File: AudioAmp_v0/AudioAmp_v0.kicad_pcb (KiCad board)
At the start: 2 copper layers, 95 x 72 mm, 4 parts

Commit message: 最低限完成
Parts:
- added C1: 100u, Capacitor_SMD:CP_Elec_6.3x5.7, F.Cu at (15.2, 15.9)
- added C10: 0.1u, Capacitor_THT:C_Rect_L13.0mm_W6.0mm_P10.00mm_FKS3_FKP3_MKS4, F.Cu at (170.3, 19.5)
- added C11: 0.1u, Capacitor_THT:C_Rect_L13.0mm_W6.0mm_P10.00mm_FKS3_FKP3_MKS4, F.Cu at (170.3, 27.0)
- added C12: 0.1u, Capacitor_SMD:C_0603_1608Metric, F.Cu at (63.5, 14.0)
- added C13: 0.1u, Capacitor_SMD:C_0603_1608Metric, F.Cu at (137.2, 86.3)
- added C14: ~, Capacitor_SMD:C_0805_2012Metric, F.Cu at (10.8, 27.9)
- added C15: ~, Capacitor_SMD:C_0805_2012Metric, F.Cu at (31.1, 30.5)
- added C16: ~, Capacitor_SMD:C_0805_2012Metric, F.Cu at (39.4, 38.7)
- added C17: ~, Capacitor_SMD:C_0805_2012Metric, F.Cu at (25.4, 51.8)
- added C18: 100u, Capacitor_SMD:CP_Elec_6.3x5.7, F.Cu at (16.5, 38.1)
- added C19: 100u, Capacitor_SMD:CP_Elec_6.3x5.7, F.Cu at (16.5, 47.6)
- added C2: 10u, Capacitor_SMD:C_0805_2012Metric, F.Cu at (22.2, 13.8)
- added C3: 0.1u, Capacitor_SMD:C_0603_1608Metric, F.Cu at (22.2, 11.9)
- added C4: 2.2u, Capacitor_THT:C_Axial_L17.0mm_D7.0mm_P20.00mm_Horizontal, F.Cu at (45.7, 51.9)
- added C5: 2.2u, Capacitor_THT:C_Axial_L17.0mm_D7.0mm_P20.00mm_Horizontal, F.Cu at (53.3, 54.5)
- added C6: 0.1u, Capacitor_SMD:C_0603_1608Metric, F.Cu at (28.4, 12.1)
- added C7: 0.1u, Capacitor_SMD:C_0603_1608Metric, F.Cu at (33.6, 12.0)
- added C8: 10u, Capacitor_SMD:C_0805_2012Metric, F.Cu at (28.4, 13.9)
- added C9: 10u, Capacitor_SMD:C_0805_2012Metric, F.Cu at (33.6, 13.8)
- added J1: AudioJack3, Connector_Audio:Jack_3.5mm_Switronic_ST-005-G_horizontal, F.Cu at (15.2, 63.5)
- added J2: Conn_01x02_Pin, Connector_Molex:Molex_SPOX_5268-02A_1x02_P2.50mm_Horizontal, F.Cu at (7.62, 12.7)
- added J3: Connector_RCJ-042, TomoshibiLibrary:Connector_RCJ-042CUD, F.Cu at (25.4, 62.3)
- added J4: Connector_RCJ-042, TomoshibiLibrary:Connector_RCJ-042CUD, F.Cu at (38.1, 62.3)
- added J5: AudioJack3, Connector_Audio:Jack_3.5mm_Switronic_ST-005-G_horizontal, F.Cu at (78.7, 63.5)
- added J6: Conn_01x02_Pin, Connector_JST:JST_XH_S2B-XH-A_1x02_P2.50mm_Horizontal, F.Cu at (9.80, 36.9)
- added J7: Conn_01x02_Pin, Connector_JST:JST_XH_S2B-XH-A_1x02_P2.50mm_Horizontal, F.Cu at (9.80, 45.7)
- added Q1: NMOS_ MTB7D0N6RJ3, Package_TO_SOT_SMD:TO-252-2, F.Cu at (26.7, 38.4)
- added Q2: PMOS_MTP4835I3, Package_TO_SOT_SMD:TO-252-2, F.Cu at (24.1, 30.7)
- added Q3: NMOS_BSS138, Package_TO_SOT_SMD:SOT-23, F.Cu at (34.9, 39.4)
- added Q4: PMOS_BSS84, Package_TO_SOT_SMD:TSOT-23, F.Cu at (15.7, 28.8)
- added Q5: PMOS_BSS84, Package_TO_SOT_SMD:TSOT-23, F.Cu at (31.1, 23.5)
- added Q6: PMOS_MTP4835I3, Package_TO_SOT_SMD:TO-252-2, F.Cu at (22.3, 23.2)
- added Q7: NMOS_BSS138, Package_TO_SOT_SMD:SOT-23, F.Cu at (21.9, 44.5)
- added Q8: NMOS_ MTB7D0N6RJ3, Package_TO_SOT_SMD:TO-252-2, F.Cu at (30.3, 45.5)
- added R1: 1K, Resistor_THT:R_Axial_DIN0207_L6.3mm_D2.5mm_P10.16mm_Horizontal, F.Cu at (45.7, 27.9)
- added R10: 27K, Resistor_THT:R_Axial_DIN0207_L6.3mm_D2.5mm_P10.16mm_Horizontal, F.Cu at (114.1, 54.2)
- added R11: 47, Resistor_THT:R_Axial_DIN0207_L6.3mm_D2.5mm_P10.16mm_Horizontal, F.Cu at (63.5, 38.1)
- added R12: 47, Resistor_THT:R_Axial_DIN0207_L6.3mm_D2.5mm_P10.16mm_Horizontal, F.Cu at (114.1, 62.3)
- added R13: 47, Resistor_THT:R_Axial_DIN0207_L6.3mm_D2.5mm_P10.16mm_Horizontal, F.Cu at (68.6, 30.5)
- added R14: 47, Resistor_THT:R_Axial_DIN0207_L6.3mm_D2.5mm_P10.16mm_Horizontal, F.Cu at (114.1, 70.4)
- added R15: 22, Resistor_THT:R_Axial_DIN0207_L6.3mm_D2.5mm_P10.16mm_Horizontal, F.Cu at (85.1, 63.5)
- added R16: 22, Resistor_THT:R_Axial_DIN0207_L6.3mm_D2.5mm_P10.16mm_Horizontal, F.Cu at (72.4, 59.7)
- added R17: 10K, Resistor_SMD:R_0603_1608Metric, F.Cu at (28.4, 15.9)
- added R18: 10K, Resistor_SMD:R_0603_1608Metric, F.Cu at (33.6, 15.8)
- added R19: 100K, Resistor_SMD:R_0603_1608Metric, F.Cu at (12.9, 27.8)
- added R2: 1K, Resistor_THT:R_Axial_DIN0207_L6.3mm_D2.5mm_P10.16mm_Horizontal, F.Cu at (114.1, 21.8)
- added R20: 10k, Resistor_SMD:R_0603_1608Metric, F.Cu at (16.5, 24.8)
- added R21: 10K, Resistor_SMD:R_0603_1608Metric, F.Cu at (15.7, 31.9)
- added R22: 10K, Resistor_SMD:R_0603_1608Metric, F.Cu at (31.1, 20.3)
- added R23: 100K, Resistor_SMD:R_0603_1608Metric, F.Cu at (31.1, 26.7)
- added R24: 10k, Resistor_SMD:R_0603_1608Metric, F.Cu at (31.1, 28.6)
- added R25: 10K, Resistor_SMD:R_0603_1608Metric, F.Cu at (34.9, 36.2)
- added R26: 100K, Resistor_SMD:R_0603_1608Metric, F.Cu at (37.5, 38.7)
- added R27: 10k, Resistor_SMD:R_0603_1608Metric, F.Cu at (36.7, 42.2)
- added R28: 10K, Resistor_SMD:R_0603_1608Metric, F.Cu at (21.9, 47.6)
- added R29: 100K, Resistor_SMD:R_0603_1608Metric, F.Cu at (25.4, 50.0)
- added R3: 22K, Resistor_THT:R_Axial_DIN0207_L6.3mm_D2.5mm_P10.16mm_Horizontal, F.Cu at (49.5, 27.9)
- added R30: 10k, Resistor_SMD:R_0603_1608Metric, F.Cu at (21.0, 40.0)
- added R4: 22K, Resistor_THT:R_Axial_DIN0207_L6.3mm_D2.5mm_P10.16mm_Horizontal, F.Cu at (114.1, 29.9)
- added R5: 2.2K, Resistor_THT:R_Axial_DIN0207_L6.3mm_D2.5mm_P10.16mm_Horizontal, F.Cu at (53.3, 27.9)
- added R6: 2.2K, Resistor_THT:R_Axial_DIN0207_L6.3mm_D2.5mm_P10.16mm_Horizontal, F.Cu at (114.1, 38.0)
- added R7: 10K, Resistor_THT:R_Axial_DIN0207_L6.3mm_D2.5mm_P10.16mm_Horizontal, F.Cu at (87.6, 33.0)
- added R8: 10K, Resistor_THT:R_Axial_DIN0207_L6.3mm_D2.5mm_P10.16mm_Horizontal, F.Cu at (114.1, 46.1)
- added R9: 27K, Resistor_THT:R_Axial_DIN0207_L6.3mm_D2.5mm_P10.16mm_Horizontal, F.Cu at (73.7, 21.6)
- added RV1: R_Potentiometer_Dual, TomoshibiLibrary:VR_ALPS9-dual, F.Cu at (55.5, 65.9)
- added SW1: SW_DPDT_x2, Button_Switch_THT:SW_CK_JS202011CQN_DPDT_Straight, F.Cu at (5.84, 22.9)
- added SW2: SW_DPDT_x2, Button_Switch_THT:SW_E-Switch_EG2219_DPDT_Angled, F.Cu at (60.8, 64.8)
- added U1: MAU108, TomoshibiLibrary:DCDC_MAUseries, F.Cu at (18.8, 4.63)
- added U2: NJM5532, Package_DIP:DIP-8_W7.62mm, F.Cu at (58.4, 19.1)
- added U3: NJM5532, Package_DIP:DIP-8_W7.62mm, F.Cu at (177.4, 73.9)
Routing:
- net Net-(J1-PadT): track 0.00 -> 40.3 mm
- net -12V: track 0.00 -> 40.3 mm
- net Net-(Q3-G): track 0.00 -> 40.2 mm, vias 0 -> 1
- net Net-(J1-PadR): track 0.00 -> 38.0 mm
- net Net-(Q7-G): track 0.00 -> 37.9 mm, vias 0 -> 1
- net Net-(Q5-G): track 0.00 -> 28.8 mm, vias 0 -> 1
- net +12V: track 0.00 -> 28.5 mm
- net +9V: track 0.00 -> 27.6 mm
- net -9V: track 0.00 -> 24.8 mm
- net Net-(Q7-D): track 0.00 -> 16.3 mm
- net GND: track 0.00 -> 15.0 mm
- net Net-(Q4-G): track 0.00 -> 11.7 mm
- net Net-(Q5-D): track 0.00 -> 10.9 mm
- net Net-(Q2-G): track 0.00 -> 10.8 mm
- net Net-(Q1-G): track 0.00 -> 10.4 mm
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- added copper zone on F.Cu, net +5V

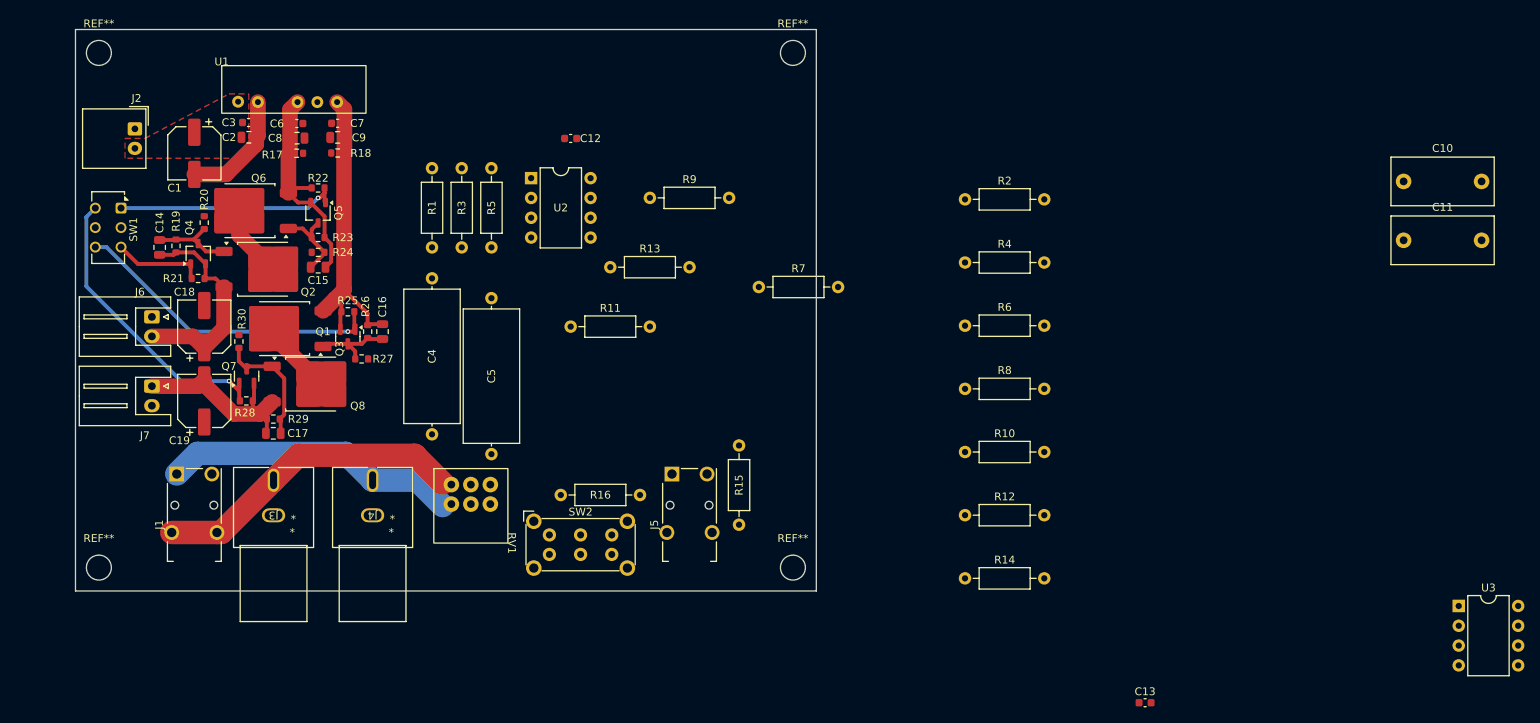
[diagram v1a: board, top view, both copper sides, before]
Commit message: LED追加
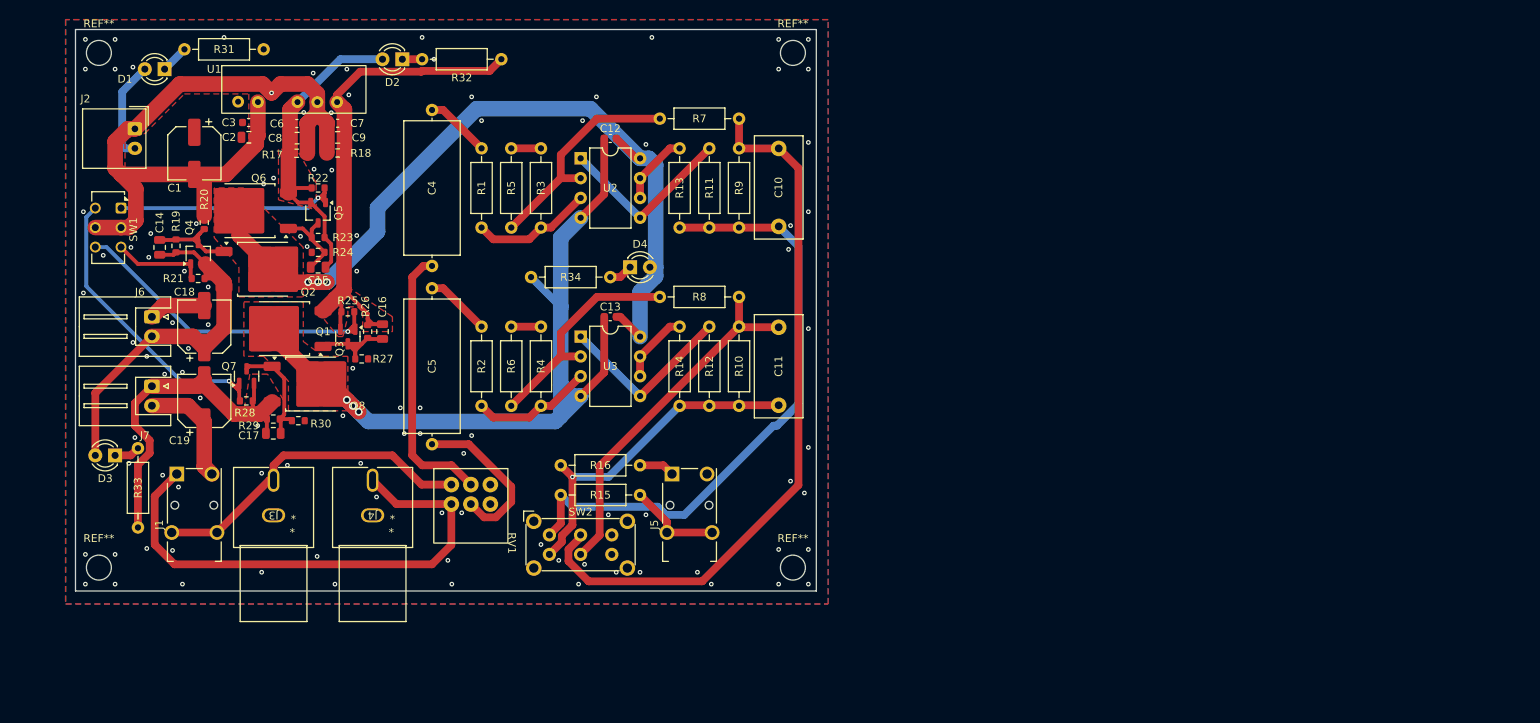
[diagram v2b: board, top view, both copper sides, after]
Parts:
- added D1: LED, LED_THT:LED_D3.0mm, F.Cu at (11.4, 5.08)
- added D2: LED, LED_THT:LED_D3.0mm, F.Cu at (41.9, 3.81)
- added D3: LED, LED_THT:LED_D3.0mm, F.Cu at (5.08, 54.6)
- added D4: LED, LED_THT:LED_D3.0mm, F.Cu at (71.1, 30.5)
- added R31: 10K, Resistor_THT:R_Axial_DIN0207_L6.3mm_D2.5mm_P10.16mm_Horizontal, F.Cu at (24.1, 2.54)
- added R32: 10K, Resistor_THT:R_Axial_DIN0207_L6.3mm_D2.5mm_P10.16mm_Horizontal, F.Cu at (54.6, 3.81)
- added R33: 10K, Resistor_THT:R_Axial_DIN0207_L6.3mm_D2.5mm_P10.16mm_Horizontal, F.Cu at (8.01, 63.9)
- added R34: 10K, Resistor_THT:R_Axial_DIN0207_L6.3mm_D2.5mm_P10.16mm_Horizontal, F.Cu at (58.4, 31.8)
- moved U3 117.8 mm to (64.8, 39.4)
- moved C13 84.6 mm to (68.6, 36.8), turned to 180 degrees
- moved C11 80.9 mm to (90.2, 38.2), turned to -90 degrees
- moved C10 80.2 mm to (90.2, 15.2), turned to -90 degrees
- moved R2 64.1 mm to (52.1, 38.1), turned to -90 degrees
- moved R6 58.2 mm to (55.9, 38.1), turned to -90 degrees
- moved R4 55.0 mm to (59.7, 38.1), turned to -90 degrees
- moved R14 42.8 mm to (77.5, 48.3), turned to 90 degrees
- moved R12 35.7 mm to (81.3, 48.3), turned to 90 degrees
- moved R8 31.3 mm to (85.1, 34.3), turned to 180 degrees
- moved R10 29.6 mm to (85.1, 48.3), turned to 90 degrees
- moved R11 21.8 mm to (81.3, 25.4), turned to 90 degrees
- moved R7 21.7 mm to (85.1, 11.4), turned to 180 degrees
- moved C4 21.6 mm to (45.7, 30.3)
- moved R3 16.3 mm to (59.7, 15.2), turned to -90 degrees
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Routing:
- net GND: track 15.0 -> 120.9 mm, vias 0 -> 102
- net VCC: track 9.30 -> 107.2 mm, vias 0 -> 3
- net VEE: track 9.62 -> 107.2 mm, vias 0 -> 3
- net Net-(SW2A-B): track 0.00 -> 92.8 mm
- net Net-(SW2A-A): track 0.00 -> 79.8 mm
- net Net-(SW2B-B): track 0.00 -> 46.5 mm
- net Net-(SW2B-A): track 0.00 -> 43.5 mm, vias 0 -> 1
- net Net-(C4-Pad1): track 0.00 -> 35.1 mm
- net Net-(U3A--): track 0.00 -> 30.9 mm
- net Net-(U2A--): track 0.00 -> 29.1 mm
- net Net-(J1-PadR): track 38.0 -> 66.9 mm
- net -12V: track 40.3 -> 65.1 mm
- net Net-(U3B-+): track 0.00 -> 23.4 mm
- net Net-(U2B-+): track 0.00 -> 23.4 mm
- net +9V: track 27.6 -> 49.8 mm
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- added copper zone on F.Cu, net +12V
- added copper zone on F.Cu, net -12V
- added copper zone on F.Cu, net -9V
- added copper zone on B.Cu, net GND
- added copper zone on F.Cu, net GND
- added copper zone on F.Cu, net VCC
- added copper zone on F.Cu, net VEE

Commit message: シルク追加
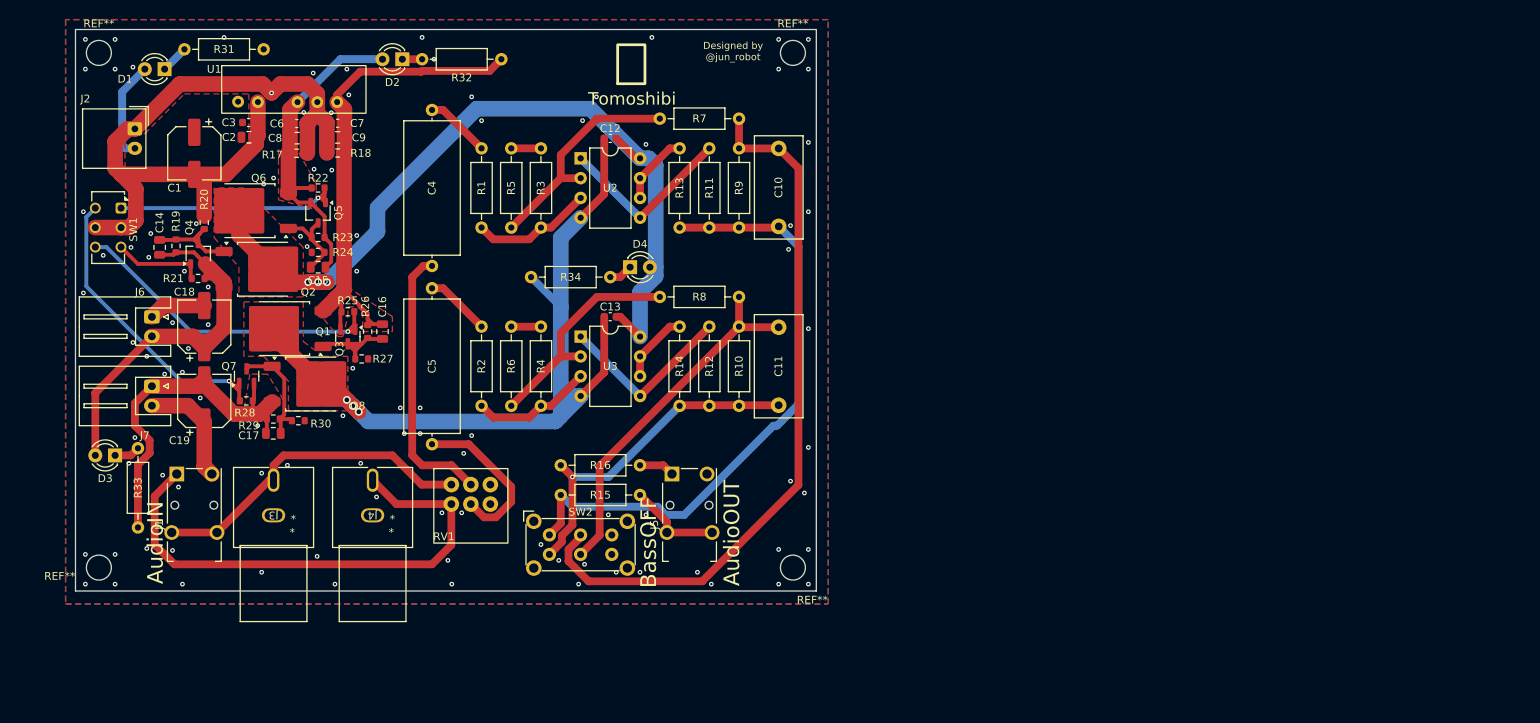
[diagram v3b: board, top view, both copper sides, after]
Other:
- board text added: "AudioIN"
- board text added: "AudioOUT"
- board text added: "BassOFF"
- board text added: "Designed by @jun_robot"
- board text added: "Tomoshibi"
- board text added: "燈"
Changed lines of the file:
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@@
     (tags "mounting hole 3.2mm no annular m3 iso14580")
     (attr exclude_from_pos_files exclude_from_bom)
-    (fp_text reference "REF**" (at 0 -3.75) (layer "F.SilkS")
+    (fp_text reference "REF**" (at -5.032 1.104) (layer "F.SilkS")
         (effects (font (size 1 1) (thickness 0.15)))
     )
@@
     (property "ki_keywords" "resistor variable")
     (attr through_hole)
-    (fp_text reference "RV1" (at 0 -0.5 -90 unlocked) (layer "F.SilkS")
+    (fp_text reference "RV1" (at -0.831 8.206 unlocked) (layer "F.SilkS")
         (effects (font (size 1 1) (thickness 0.1)))
     )
@@
     (tags "mounting hole 3.2mm no annular m3 iso14580")
     (attr exclude_from_pos_files exclude_from_bom)
-    (fp_text reference "REF**" (at 0 -3.75) (layer "F.SilkS")
+    (fp_text reference "REF**" (at 2.488 4.152) (layer "F.SilkS")
         (effects (font (size 1 1) (thickness 0.15)))
     )
@@
   (gr_rect (start 0 0) (end 95 72)
     (stroke (width 0.05) (type default)) (fill none) (layer "Edge.Cuts"))
+  (gr_text "AudioIN" (at 11.43 71.12 90) (layer "F.SilkS" knockout)
+    (effects (font (size 2 2) (thickness 0.3)) (justify left bottom))
+  )
+  (gr_text "Designed by\n@jun_robot" (at 84.328 2.794) (layer "F.SilkS")
+    (effects (font (size 0.9 0.9) (thickness 0.11)))
+  )
+  (gr_text "BassOFF\n" (at 74.676 71.628 90) (layer "F.SilkS" knockout)
+    (effects (font (size 2 2) (thickness 0.3)) (justify left bottom))
+  )
+  (gr_text "燈" (at 71.274 4.64) (layer "F.SilkS")
+    (effects (font (size 5 5) (thickness 0.35)))
+  )
+  (gr_text "AudioOUT" (at 85.344 71.374 90) (layer "F.SilkS" knockout)
+    (effects (font (size 2 2) (thickness 0.3)) (justify left bottom))
+  )
+  (gr_text "Tomoshibi" (at 71.374 8.89) (layer "F.SilkS")
+    (effects (font (size 1.6 1.6) (thickness 0.21)))
+  )
   (segment (start 8.89 5.08) (end 5.995 7.975) (width 1) (layer "B.Cu") (net 1))
   (segment (start 5.995 14.885) (end 6.35 15.24) (width 1) (layer "B.Cu") (net 1))

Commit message: 電源切り替えスイッチ修正
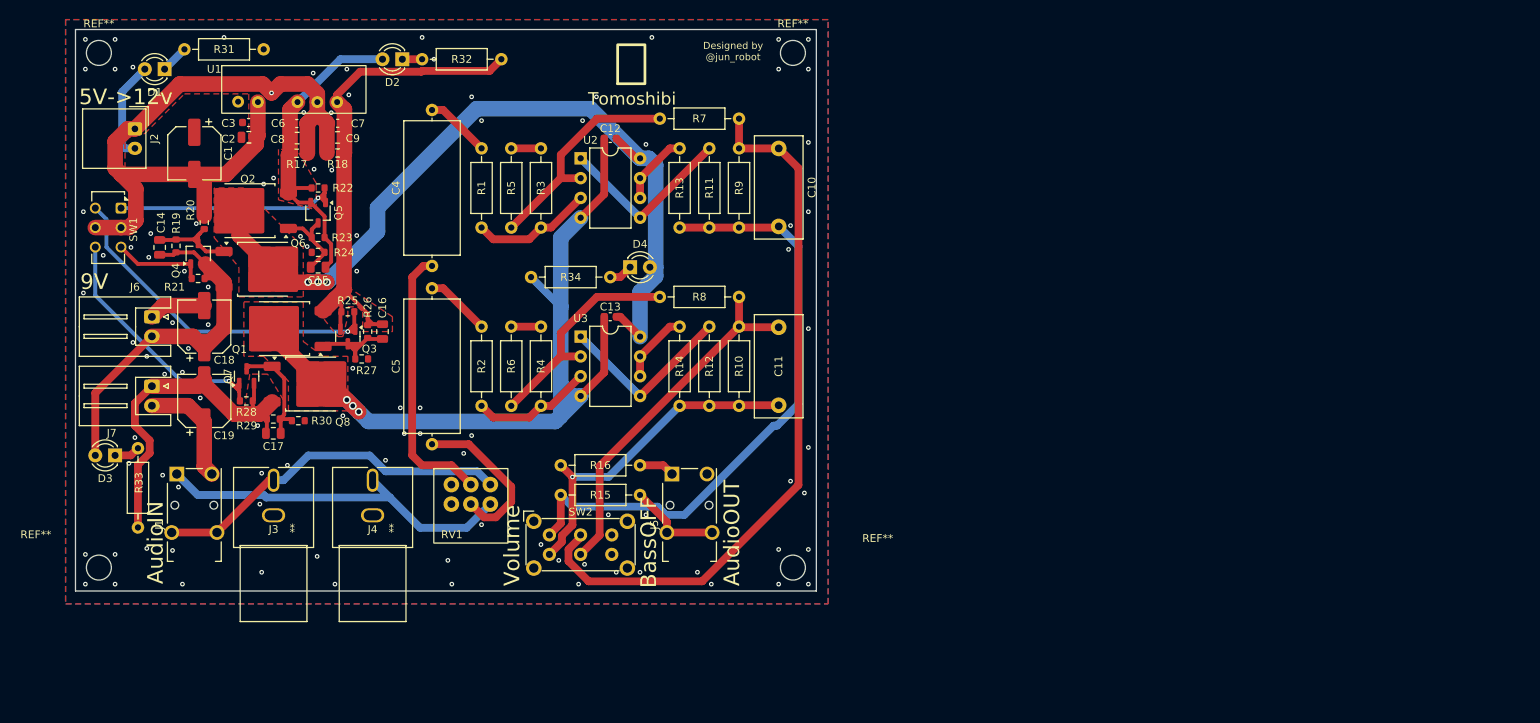
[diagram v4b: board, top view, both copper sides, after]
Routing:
- net Net-(J1-PadR): track 66.9 -> 47.5 mm
- net Net-(Q7-G): track 38.7 -> 32.8 mm
- net Net-(Q3-G): track 41.3 -> 45.5 mm
- net Net-(J1-PadT): track 42.6 -> 46.5 mm
- net GND: vias 102 -> 101
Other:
- board text added: "5V->12v"
- board text added: "9V"
- board text added: "Volume"
